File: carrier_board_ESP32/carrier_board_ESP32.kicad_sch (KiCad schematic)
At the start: 45 parts, among them IC1 SS49E, IC2 SS49E, IC3 SS49E, IC4 SS49E, IC5 SS49E, IC6 SS49E, IC7 DRV5023, IC8 DRV5023, J1 BME280, J2 LTR390, J3 ENS160 I2C, J4 ENS160 SPI, J5 ENS160 + AHT21, J6 Conn_01x02_Socket, J7 Conn_01x02_Socket, J8 UJC-HP-3-SMT-TR, U1 ESP32-S3-DEVKITC-1-N8R2, U2 TP4056, U3 LM2576HVS-5, U4 MT3608

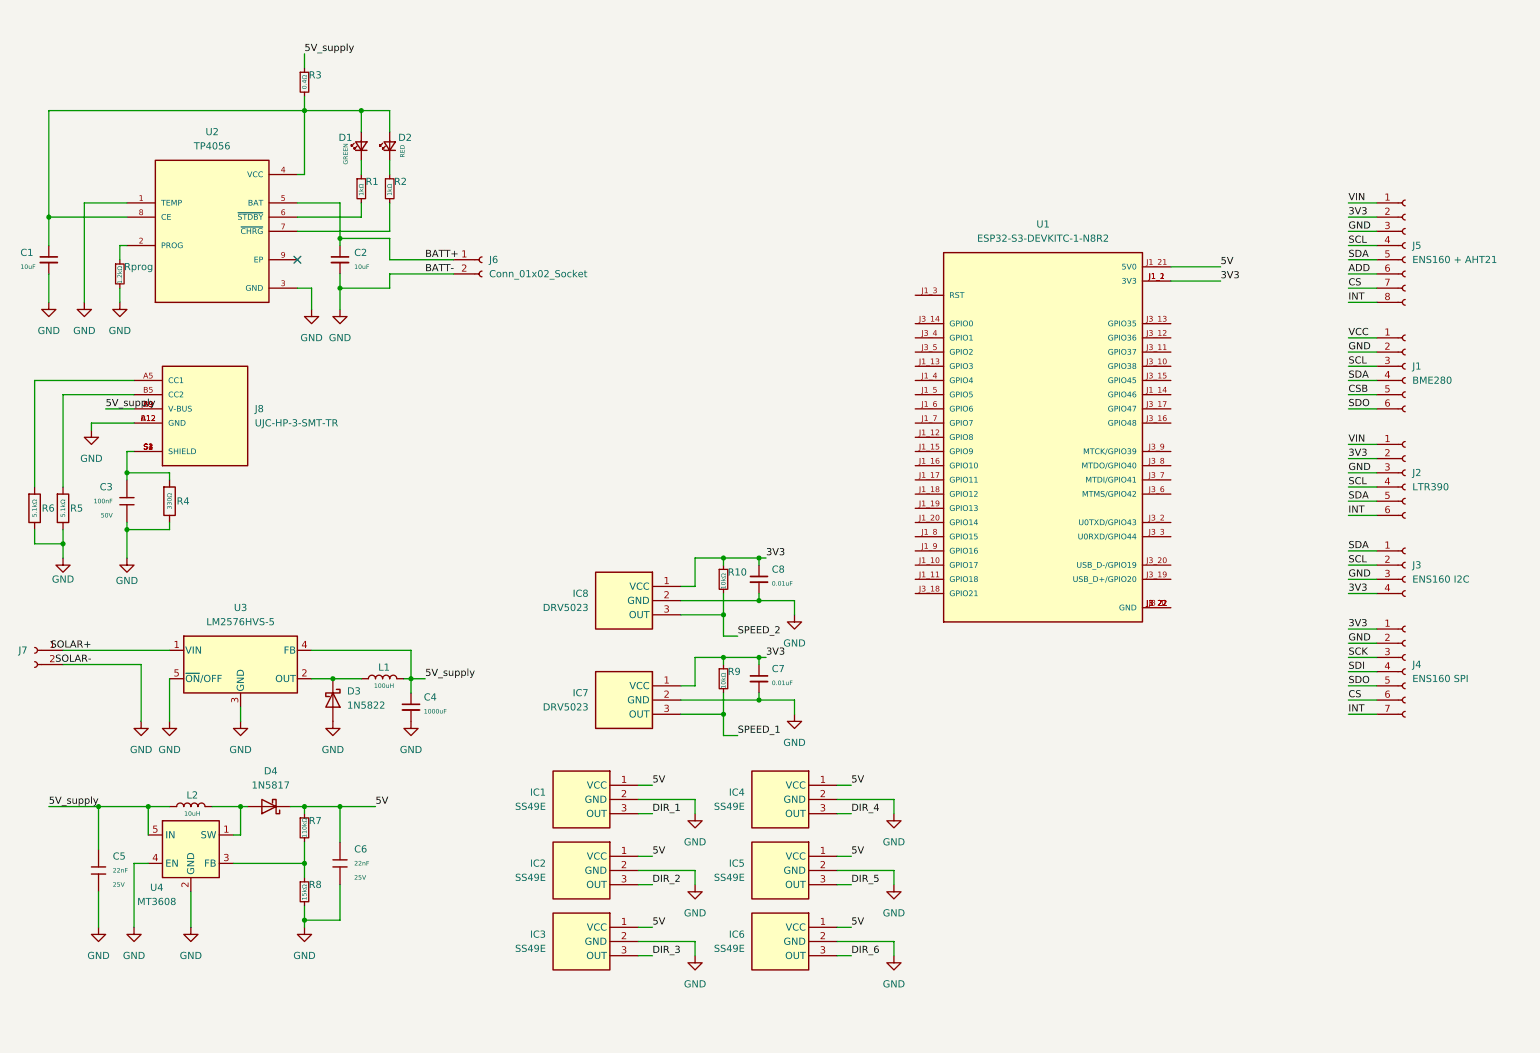
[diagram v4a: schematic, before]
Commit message: completed escheme without rain detector
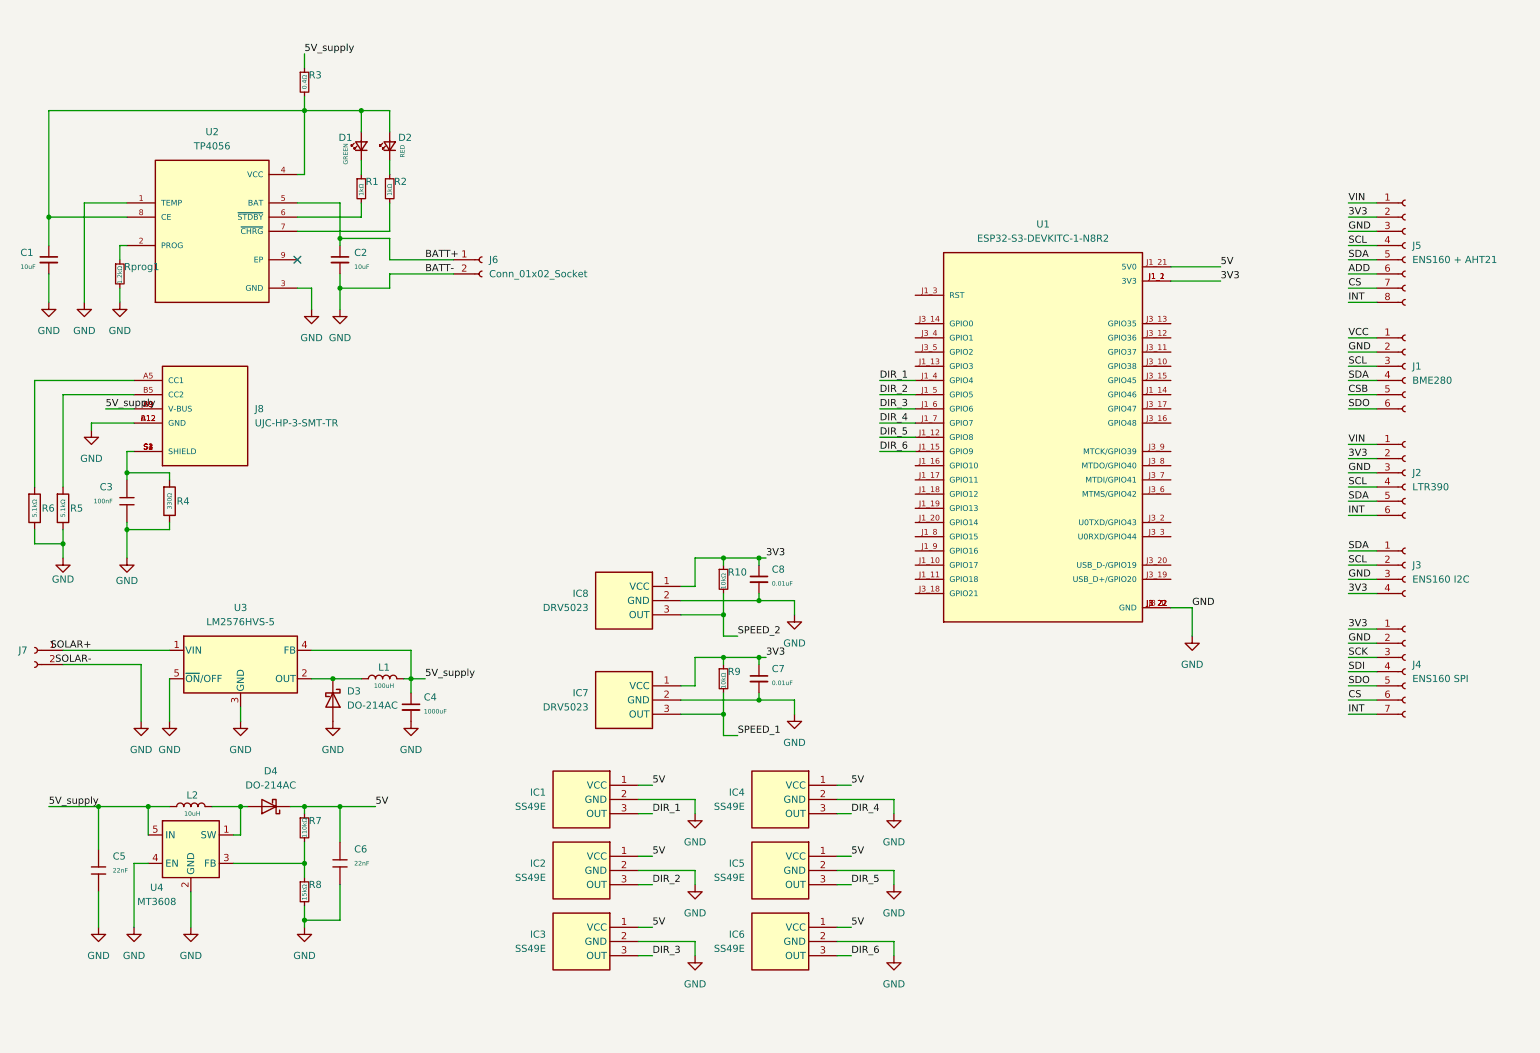
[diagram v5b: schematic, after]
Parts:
- removed D3: 1N5822, Diode_THT:D_DO-201AD_P15.24mm_Horizontal, symbol Diode:1N5822
- added D3: DO-214AC, Diode_SMD:D_SMA_Handsoldering, symbol Diode:1N5817
- C1, C2, C4, C7, C8: footprint (none) -> Capacitor_SMD:C_0805_2012Metric_Pad1.18x1.45mm_HandSolder
- C3: footprint PCM_JLCPCB:C_0402 -> Capacitor_SMD:C_0805_2012Metric_Pad1.18x1.45mm_HandSolder; Attrition Qty 10 -> (none); Capacitance 100nF -> (none); Category Capacitors,Multilayer Ceramic Capacitors MLCC - SMD/SMT -> (none); Class Basic Component -> (none); LCSC C307331 -> (none); Manufacturer Samsung Electro-Mechanics -> (none); Minimum Qty 20 -> (none); Part CL05B104KB54PNC -> (none); Price 0.008USD -> (none); Process SMT -> (none); Stock 3851753 -> (none); Temperature Coefficient X7R -> (none); Tolerance ±10% -> (none); Voltage Rated 50V -> (none)
- C5, C6: footprint PCM_JLCPCB:C_0402 -> Capacitor_SMD:C_0805_2012Metric_Pad1.18x1.45mm_HandSolder; Attrition Qty 10 -> (none); Capacitance 100nF -> (none); Category Capacitors,Multilayer Ceramic Capacitors MLCC - SMD/SMT -> (none); Class Basic Component -> (none); LCSC C307331 -> (none); Manufacturer Samsung Electro-Mechanics -> (none); Minimum Qty 20 -> (none); Part CL05B104KB54PNC -> (none); Price 0.008USD -> (none); Process SMT -> (none); Stock 3851753 -> (none); Temperature Coefficient X7R -> (none); Tolerance ±10% -> (none); Voltage Rated 25V -> (none)
- D1, D2: footprint (none) -> LED_SMD:LED_0805_2012Metric_Pad1.15x1.40mm_HandSolder
- D4: value 1N5817 -> DO-214AC; footprint Diode_THT:D_DO-41_SOD81_P10.16mm_Horizontal -> Diode_SMD:D_SMA_Handsoldering
- J1, J2: footprint Connector_PinHeader_1.00mm:PinHeader_1x06_P1.00mm_Vertical -> Connector_PinHeader_2.54mm:PinHeader_1x06_P2.54mm_Vertical
- J3: footprint Connector_PinHeader_1.00mm:PinHeader_1x04_P1.00mm_Vertical -> Connector_PinHeader_2.54mm:PinHeader_1x04_P2.54mm_Vertical
- J4: footprint Connector_PinHeader_1.00mm:PinHeader_1x07_P1.00mm_Vertical -> Connector_PinHeader_2.54mm:PinHeader_1x07_P2.54mm_Vertical
- J5: footprint Connector_PinHeader_1.00mm:PinHeader_1x08_P1.00mm_Vertical -> Connector_PinHeader_2.54mm:PinHeader_1x08_P2.54mm_Vertical
- L1: footprint (none) -> ESP32-S3-DEVKITC-1-N8R2:INDPM125125X800N
- L2: footprint (none) -> Inductor_SMD:L_Bourns_SRR1260
- R1, R10, R2, R3, R7, R8, R9: footprint (none) -> Resistor_SMD:R_0805_2012Metric_Pad1.20x1.40mm_HandSolder
- R4: footprint PCM_JLCPCB:R_0402 -> Resistor_SMD:R_0805_2012Metric_Pad1.20x1.40mm_HandSolder; Attrition Qty 10 -> (none); Category Resistors,Chip Resistor - Surface Mount -> (none); Class Basic Component -> (none); LCSC C25104 -> (none); Manufacturer UNI-ROYAL(Uniroyal Elec) -> (none); Minimum Qty 20 -> (none); Operating Temperature Range -55°C~+155°C -> (none); Overload Voltage (Max) 50V -> (none); Part 0402WGF3300TCE -> (none); Power(Watts) 62.5mW -> (none); Price 0.004USD -> (none); Process SMT -> (none); Resistance 330Ω -> (none); Stock 399284 -> (none); Temperature Coefficient ±100ppm/°C -> (none); Tolerance ±1% -> (none); Type Thick Film Resistors -> (none)
- R5, R6: footprint PCM_JLCPCB:R_0402 -> Resistor_SMD:R_0805_2012Metric_Pad1.20x1.40mm_HandSolder; Attrition Qty 10 -> (none); Category Resistors,Chip Resistor - Surface Mount -> (none); Class Basic Component -> (none); LCSC C25905 -> (none); Manufacturer UNI-ROYAL(Uniroyal Elec) -> (none); Minimum Qty 20 -> (none); Operating Temperature Range -55°C~+155°C -> (none); Overload Voltage (Max) 50V -> (none); Part 0402WGF5101TCE -> (none); Power(Watts) 62.5mW -> (none); Price 0.004USD -> (none); Process SMT -> (none); Resistance 5.1kΩ -> (none); Stock 2022176 -> (none); Temperature Coefficient ±100ppm/°C -> (none); Tolerance ±1% -> (none); Type Thick Film Resistors -> (none)
- Rprog1: renamed from Rprog; footprint (none) -> Resistor_SMD:R_0805_2012Metric_Pad1.20x1.40mm_HandSolder
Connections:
- net DIR_1: now also U1.J1_4 (GPIO4)
- net DIR_2: now also U1.J1_5 (GPIO5)
- net DIR_3: now also U1.J1_6 (GPIO6)
- net DIR_4: now also U1.J1_7 (GPIO7)
- net DIR_5: now also U1.J1_12 (GPIO8)
- net DIR_6: now also U1.J1_15 (GPIO9)
- net GND: now also U1.J1_22 (GND), U1.J3_1 (GND), U1.J3_21 (GND), U1.J3_22 (GND), D3.2 (A)
- net at L1.1, U3.2 (OUT): now also D3.1 (K)

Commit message: formated file, ready for check
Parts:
- removed C7, C8: 0.01uF, Capacitor_SMD:C_0805_2012Metric_Pad1.18x1.45mm_HandSolder, symbol Device:C_Small
- added J10, J11, J12, J13, J14, J15, J16, J9: Conn_01x03_Socket, Connector_PinHeader_2.54mm:PinHeader_1x03_P2.54mm_Vertical, symbol Connector:Conn_01x03_Socket
- added J17, J18: Conn_01x22_Socket, symbol Connector:Conn_01x22_Socket
- added R11, R13: 1kΩ, Resistor_SMD:R_0805_2012Metric_Pad1.20x1.40mm_HandSolder, symbol Device:R_Small
- added R12, R14: 2kΩ, Resistor_SMD:R_0805_2012Metric_Pad1.20x1.40mm_HandSolder, symbol Device:R_Small
- IC7, IC8: value DRV5023 -> A3144
- R10, R9: value 10kΩ -> 4k7Ω
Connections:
- net CSB is gone; now on net 3V3: J1.5 (Pin_5)
- net VCC is gone; now on net 3V3: J1.1 (Pin_1)
- net 3V3: now also J1.6 (Pin_6), J2.1 (Pin_1), J17.1 (Pin_1), J17.2 (Pin_2); no longer IC7.1 (VCC), IC8.1 (VCC), J2.2 (Pin_2), R10.1, R9.1
- net 5V: now also IC7.1 (VCC), IC8.1 (VCC), R10.1, R9.1, J10.1 (Pin_1), J11.1 (Pin_1), J12.1 (Pin_1), J13.1 (Pin_1), J14.1 (Pin_1), J15.1 (Pin_1), J16.1 (Pin_1), J17.21 (Pin_21), J9.1 (Pin_1)
- net CS: now also U1.J1_16 (GPIO10), J17.16 (Pin_16)
- net DIR_1: now also J17.4 (Pin_4), J9.3 (Pin_3)
- net DIR_2: now also J10.3 (Pin_3), J17.5 (Pin_5)
- net DIR_3: now also J11.3 (Pin_3), J17.6 (Pin_6)
- net DIR_4: now also J12.3 (Pin_3), J17.7 (Pin_7)
- net DIR_5: now also U1.J1_8 (GPIO15), J13.3 (Pin_3), J17.8 (Pin_8); no longer U1.J1_12 (GPIO8)
- net DIR_6: now also U1.J1_9 (GPIO16), J14.3 (Pin_3), J17.9 (Pin_9); no longer U1.J1_15 (GPIO9)
- net GND: now also J10.2 (Pin_2), J11.2 (Pin_2), J12.2 (Pin_2), J13.2 (Pin_2), J14.2 (Pin_2), J15.2 (Pin_2), J16.2 (Pin_2), J17.22 (Pin_22), J18.1 (Pin_1), J18.21 (Pin_21), J18.22 (Pin_22), J9.2 (Pin_2), R12.2, R14.2
- net INT: now also U1.J1_20 (GPIO14)
- net SCK: now also U1.J1_18 (GPIO12), J17.18 (Pin_18)
- net SCL: now also U1.J1_15 (GPIO9), J17.15 (Pin_15)
- net SDA: now also U1.J1_12 (GPIO8), J17.12 (Pin_12)
- net SDO: no longer J1.6 (Pin_6)
- net SPEED_1: now also U1.J3_4 (GPIO1), J15.3 (Pin_3), J18.4 (Pin_4), R13.2, R14.1; no longer IC7.3 (OUT), R9.2
- net SPEED_2: now also U1.J3_5 (GPIO2), J16.3 (Pin_3), J18.5 (Pin_5), R11.2, R12.1; no longer IC8.3 (OUT), R10.2
- net VIN: no longer J2.1 (Pin_1)
- net GPIO17: now reaches U1.J1_10 (GPIO17)
- net GPIO17: now also J17.10 (Pin_10)
- net GPIO18: now reaches U1.J1_11 (GPIO18)
- net GPIO18: now also J17.11 (Pin_11)
- net GPIO3: now reaches U1.J1_13 (GPIO3)
- net GPIO3: now also J17.13 (Pin_13)
- net GPIO46: now reaches U1.J1_14 (GPIO46)
- net GPIO46: now also J17.14 (Pin_14)
- net MOSI: now reaches U1.J1_17 (GPIO11)
- net MOSI: now also J17.17 (Pin_17)
- net MISO: now reaches U1.J1_19 (GPIO13)
- net MISO: now also J17.19 (Pin_19)
- net RST: now reaches U1.J1_3 (RST)
- net RST: now also J17.3 (Pin_3)
- net GPIO38: now reaches U1.J3_10 (GPIO38)
- net GPIO38: now also J18.10 (Pin_10)
- net GPIO37: now reaches U1.J3_11 (GPIO37)
- net GPIO37: now also J18.11 (Pin_11)
- net GPIO36: now reaches U1.J3_12 (GPIO36)
- net GPIO36: now also J18.12 (Pin_12)
- net GPIO35: now reaches U1.J3_13 (GPIO35)
- net GPIO35: now also J18.13 (Pin_13)
- net GPIO0: now reaches U1.J3_14 (GPIO0)
- net GPIO0: now also J18.14 (Pin_14)
- net GPIO45: now reaches U1.J3_15 (GPIO45)
- net GPIO45: now also J18.15 (Pin_15)
- net GPIO48: now reaches U1.J3_16 (GPIO48)
- net GPIO48: now also J18.16 (Pin_16)
- net GPIO47: now reaches U1.J3_17 (GPIO47)
- net GPIO47: now also J18.17 (Pin_17)
- net GPIO21: now reaches U1.J3_18 (GPIO21)
- net GPIO21: now also J18.18 (Pin_18)
- net GPIO20: now reaches U1.J3_19 (USB_D+/GPIO20)
- net GPIO20: now also J18.19 (Pin_19)
- net TX: now reaches U1.J3_2 (U0TXD/GPIO43)
- net TX: now also J18.2 (Pin_2)
- net GPIO19: now reaches U1.J3_20 (USB_D-/GPIO19)
- net GPIO19: now also J18.20 (Pin_20)
- net RX: now reaches U1.J3_3 (U0RXD/GPIO44)
- net RX: now also J18.3 (Pin_3)
- net GPIO42: now reaches U1.J3_6 (MTMS/GPIO42)
- net GPIO42: now also J18.6 (Pin_6)
- net GPIO41: now reaches U1.J3_7 (MTDI/GPIO41)
- net GPIO41: now also J18.7 (Pin_7)
- net GPIO40: now reaches U1.J3_8 (MTDO/GPIO40)
- net GPIO40: now also J18.8 (Pin_8)
- net GPIO39: now reaches U1.J3_9 (MTCK/GPIO39)
- net GPIO39: now also J18.9 (Pin_9)
- new net: IC7.3 (OUT), R13.1, R9.2
- new net: IC8.3 (OUT), R10.2, R11.1
- new net GPIO14: J17.20 (Pin_20)
- no-connect marks 1 -> 2
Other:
- note added: "5V Boost Converter"
- note added: "5V Step-Down Converter"
- note added: "Battery Charging Circuit"
- note added: "ESP32-S3 Core"
- note added: "Hall Sensors (Wind Direction)"
- note added: "Hall Sensors (Wind Speed)"
- note added: "Hall Sensors Connectors"
- note added: "Sensor Header"
- note added: "USB Power Input + Protection"
- company: (none) -> Adam Prystupa 275496
- title: (none) -> ESP32-S3 carrier board
- moved on the sheet: C3, C4, C5, C6, D3, D4, IC1, IC2, IC3, IC4, IC5, IC6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

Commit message: pcb changes
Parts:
- C3: renamed from C4; footprint Capacitor_SMD:C_0805_2012Metric_Pad1.18x1.45mm_HandSolder -> Capacitor_SMD:C_Elec_10x10.2
- IC1: renamed from IC8; footprint TO130P160X410X300-3P -> Connector_PinHeader_2.54mm:PinHeader_1x03_P2.54mm_Vertical
- IC2: renamed from IC7; footprint TO130P160X410X300-3P -> Connector_PinHeader_2.54mm:PinHeader_1x03_P2.54mm_Vertical
- J1: renamed from J6; footprint Connector_AMASS:AMASS_XT30UPB-F_1x02_P5.0mm_Vertical -> Connector_AMASS:AMASS_XT30PW-M_1x02_P2.50mm_Horizontal
- J17, J18: footprint (none) -> Connector_PinHeader_2.54mm:PinHeader_1x22_P2.54mm_Vertical
- J2: renamed from J7; footprint Connector_AMASS:AMASS_XT30UPB-F_1x02_P5.0mm_Vertical -> Connector_AMASS:AMASS_XT30PW-M_1x02_P2.50mm_Horizontal
- renumbered C6 to C4, C3 to C6, D2 to CHRG1, D3 to D1, D4 to D2, J9 to DIR1, J10 to DIR2, J11 to DIR3, J12 to DIR4, J13 to DIR5, J14 to DIR6, IC1 to IC3, IC2 to IC5, IC5 to IC6, IC3 to IC7, IC6 to IC8, J2 to J12, J1 to J13, J4 to J14, J5 to J15, J3 to J16, J8 to J3, R3 to R1, R11 to R10, R12 to R11, R9 to R12, R1 to R2, R2 to R3, R7 to R4, R8 to R5, R4 to R6, R6 to R7, R5 to R8, R10 to R9, J15 to SPEED1, J16 to SPEED2, D1 to STDBY1, U2 to U1, U3 to U2, U4 to U3, U1 to U4
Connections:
- net ADD is gone; now on net MISO: J15.6 (Pin_6)
- net SDI is gone; now on net MOSI: J14.4 (Pin_4)
- net SDO is gone; now on net MISO: J14.5 (Pin_5)
- net VIN is gone; now on net 3V3: J15.1 (Pin_1)
- net 3V3: now also J16.1 (Pin_1); no longer J15.2 (Pin_2), J16.4 (Pin_4)
- net BATT+: now also J1.2 (Pin_2); no longer J1.1 (Pin_1)
- net GND: now also J1.1 (Pin_1), J16.2 (Pin_2), J2.1 (Pin_1); no longer J1.2 (Pin_2), J16.3 (Pin_3), J2.2 (Pin_2)
- net MOSI: now also J15.5 (Pin_5)
- net SCK: now also J15.4 (Pin_4)
- net SCL: now also J16.3 (Pin_3); no longer J15.4 (Pin_4), J16.2 (Pin_2)
- net SDA: now also J16.4 (Pin_4); no longer J15.5 (Pin_5), J16.1 (Pin_1)
- net SOLAR+: now also J2.2 (Pin_2); no longer J2.1 (Pin_1)
- net SPEED_1: no longer SPEED1.3 (Pin_3)
- net SPEED_2: no longer SPEED2.3 (Pin_3)
- net OUT1: now reaches IC2.3 (OUT), R12.2, R13.1
- net OUT1: now also SPEED1.3 (Pin_3)
- net OUT2: now reaches IC1.3 (OUT), R10.1, R9.2
- net OUT2: now also SPEED2.3 (Pin_3)
- net CS renamed INT_3
- net INT_3: now also J14.7 (Pin_7); no longer J14.6 (Pin_6), J15.7 (Pin_7)
- net GPIO14 renamed INT_2
- net INT_2: now also J12.6 (Pin_6), U4.J1_20 (GPIO14)
- net GPIO18 renamed CS_1
- net CS_1: now also J15.7 (Pin_7)
- net GPIO3 renamed INT_1
- net INT_1: now also J15.8 (Pin_8)
- net GPIO46 renamed CS_3
- net CS_3: now also J14.6 (Pin_6)
- removed net INT: J12.6 (Pin_6), J14.7 (Pin_7), J15.8 (Pin_8), U4.J1_20 (GPIO14)
- no-connect marks 2 -> 3
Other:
- moved on the sheet: J1, J2

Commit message: updated scheme and PCB ready for inspection
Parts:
- added C10, C15, C16, C17, C8: 10uF, Capacitor_SMD:C_0805_2012Metric_Pad1.18x1.45mm_HandSolder, symbol Device:C_Small
- added C11: 47uF, Capacitor_SMD:C_0805_2012Metric_Pad1.18x1.45mm_HandSolder, symbol Device:C_Small
- added C12: 2200uF, Capacitor_SMD:CP_Elec_10x10.5, symbol Device:C_Small
- added C13: 10uF, Capacitor_Tantalum_SMD:CP_EIA-7343-15_Kemet-W_Pad2.25x2.55mm_HandSolder, symbol Device:C_Small
- added C14: 1uF, Capacitor_SMD:C_0805_2012Metric_Pad1.18x1.45mm_HandSolder, symbol Device:C_Small
- added C7, C9: 100uF, Capacitor_Tantalum_SMD:CP_EIA-7343-15_Kemet-W_Pad2.25x2.55mm_HandSolder, symbol Device:C_Small
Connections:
- net 5V: now also C3.1, C11.1, C15.1, C16.1, C17.1
- net 5V_supply: now also C10.1, C12.1, C13.1, C14.1, C9.1; no longer C3.1
- net GND: now also C10.2, C11.2, C12.2, C13.2, C14.2, C15.2, C16.2, C17.2, C7.2, C8.2, C9.2
- net SOLAR+: now also C7.1, C8.1
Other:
- moved on the sheet: C3, C4, C5, C6, D2, J3, L2, R4, R5, R6, U3
